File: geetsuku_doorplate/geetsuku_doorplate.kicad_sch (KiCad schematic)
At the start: 3 parts

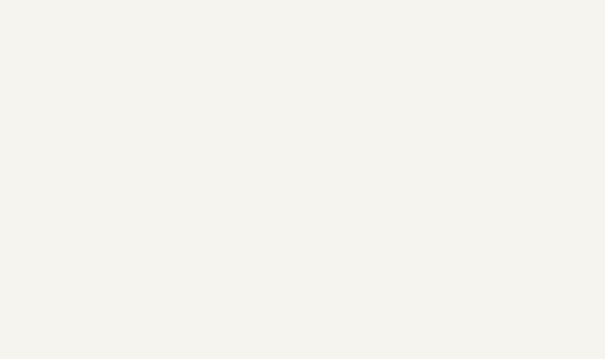
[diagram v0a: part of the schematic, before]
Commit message: add v1.2
1.1 add hole x4
1.2 change font, kicad font -> ubuntu with Bold
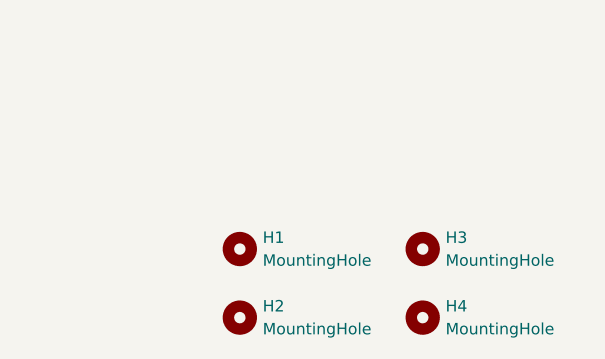
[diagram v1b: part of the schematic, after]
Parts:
- added H1, H2, H3, H4: MountingHole, MountingHole:MountingHole_6.4mm_M6, symbol Mechanical:MountingHole
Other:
- company: Geekhouse Tsukuba -> takurx
- title: (none) -> geetsuku doorplate pcb
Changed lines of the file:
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@@
   (paper "A4")
   (title_block
-    (date "2023-08-19")
-    (rev "1.0")
-    (company "Geekhouse Tsukuba")
+    (title "geetsuku doorplate pcb")
+    (date "2023-08-23")
+    (rev "1.1")
+    (company "takurx")
+    (comment 1 "1.1, add hole x4")
   )
   (junction (at 130.81 55.88) (diameter 0) (color 0 0 0 0)
@@
   (wire (pts (xy 149.86 76.2) (xy 149.86 83.82))
     (stroke (width 0) (type default))
+  )
+  (symbol (lib_id "Mechanical:MountingHole") (at 243.84 160.02 0) (unit 1)
+    (in_bom yes) (on_board yes) (dnp no) (fields_autoplaced)
+    (property "Reference" "H2" (at 246.38 158.75 0)
+      (effects (font (size 1.27 1.27)) (justify left))
+    )
+    (property "Value" "MountingHole" (at 246.38 161.29 0)
+      (effects (font (size 1.27 1.27)) (justify left))
+    )
+    (property "Footprint" "MountingHole:MountingHole_6.4mm_M6" (at 243.84 160.02 0)
+      (effects (font (size 1.27 1.27)) hide)
+    )
+    (property "Datasheet" "~" (at 243.84 160.02 0)
+      (effects (font (size 1.27 1.27)) hide)
+    )
+    (instances
+      (project "geetsuku_doorplate"
+        (path "/7d68ca57-1675-47b8-bd5b-3c8993e37635"
+          (reference "H2") (unit 1)
+        )
+      )
+    )
+  )
+  (symbol (lib_id "Mechanical:MountingHole") (at 264.16 152.4 0) (unit 1)
+    (in_bom yes) (on_board yes) (dnp no) (fields_autoplaced)
+    (property "Reference" "H3" (at 266.7 151.13 0)
+      (effects (font (size 1.27 1.27)) (justify left))
+    )
+    (property "Value" "MountingHole" (at 266.7 153.67 0)
+      (effects (font (size 1.27 1.27)) (justify left))
+    )
+    (property "Footprint" "MountingHole:MountingHole_6.4mm_M6" (at 264.16 152.4 0)
+      (effects (font (size 1.27 1.27)) hide)
+    )
+    (property "Datasheet" "~" (at 264.16 152.4 0)
+      (effects (font (size 1.27 1.27)) hide)
+    )
+    (instances
+      (project "geetsuku_doorplate"
+        (path "/7d68ca57-1675-47b8-bd5b-3c8993e37635"
+          (reference "H3") (unit 1)
+        )
+      )
+    )
   )
   (symbol (lib_id "Device:Battery") (at 130.81 80.01 0) (unit 1)
@@
     )
   )
+  (symbol (lib_id "Mechanical:MountingHole") (at 243.84 152.4 0) (unit 1)
+    (in_bom yes) (on_board yes) (dnp no) (fields_autoplaced)
+    (property "Reference" "H1" (at 246.38 151.13 0)
+      (effects (font (size 1.27 1.27)) (justify left))
+    )
+    (property "Value" "MountingHole" (at 246.38 153.67 0)
+      (effects (font (size 1.27 1.27)) (justify left))
+    )
+    (property "Footprint" "MountingHole:MountingHole_6.4mm_M6" (at 243.84 152.4 0)
+      (effects (font (size 1.27 1.27)) hide)
+    )
+    (property "Datasheet" "~" (at 243.84 152.4 0)
+      (effects (font (size 1.27 1.27)) hide)
+    )
+    (instances
+      (project "geetsuku_doorplate"
+        (path "/7d68ca57-1675-47b8-bd5b-3c8993e37635"
+          (reference "H1") (unit 1)
+        )
+      )
+    )
+  )
   (symbol (lib_id "Device:D") (at 149.86 72.39 90) (unit 1)
     (in_bom yes) (on_board yes) (dnp no) (fields_autoplaced)
@@
         )
       )
+    )
+  )
+  (symbol (lib_id "Mechanical:MountingHole") (at 264.16 160.02 0) (unit 1)
+    (in_bom yes) (on_board yes) (dnp no) (fields_autoplaced)
+    (property "Reference" "H4" (at 266.7 158.75 0)
+      (effects (font (size 1.27 1.27)) (justify left))
+    )
+    (property "Value" "MountingHole" (at 266.7 161.29 0)
+      (effects (font (size 1.27 1.27)) (justify left))
+    )
+    (property "Footprint" "MountingHole:MountingHole_6.4mm_M6" (at 264.16 160.02 0)
+      (effects (font (size 1.27 1.27)) hide)
+    )
+    (property "Datasheet" "~" (at 264.16 160.02 0)
+      (effects (font (size 1.27 1.27)) hide)
+    )
+    (instances
+      (project "geetsuku_doorplate"
+        (path "/7d68ca57-1675-47b8-bd5b-3c8993e37635"
+          (reference "H4") (unit 1)
+        )
+      )
